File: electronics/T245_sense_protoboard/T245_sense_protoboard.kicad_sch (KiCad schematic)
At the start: 2 parts

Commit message: WIP placement
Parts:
- added C1, C2, C3, C4, C5, C6, C7, C8, C9: 1u, SquantorCapacitor:C_0603, symbol Device:C
- added D1, D2: ~, SquantorIC:SOT23-3, symbol SquantorDiodes:shottky_series
- added J1: Conn_01x06, Connector_Molex:Molex_KK-254_AE-6410-06A_1x06_P2.54mm_Vertical, symbol Connector_Generic:Conn_01x06
- added J2: Conn_02x03_Odd_Even, Connector_Molex:Molex_Micro-Fit_3.0_43045-0612_2x03_P3.00mm_Vertical, symbol Connector_Generic:Conn_02x03_Odd_Even
- added R1, R10, R2, R3, R4: 22K6, SquantorResistor:R_0603_hand, symbol Device:R
- added R11, R12: 10K, SquantorResistor:R_0603_hand, symbol Device:R
- added R13: 187K, SquantorResistor:R_0603_hand, symbol Device:R
- added R14: 3K3, SquantorResistor:R_0603_hand, symbol Device:R
- added R15: 2K2, SquantorResistor:R_0603_hand, symbol Device:R
- added R16, R17: 200K, SquantorResistor:R_0603_hand, symbol Device:R
- added R18, R19: 4k75, SquantorResistor:R_0603_hand, symbol Device:R
- added R20, R21: 0R22, SquantorResistor:R_0805, symbol Device:R
- added R5, R6: 590K, SquantorResistor:R_0603_hand, symbol Device:R
- added R7: 82K, SquantorResistor:R_0603_hand, symbol Device:R
- added R8, R9: 2K7, SquantorResistor:R_0603_hand, symbol Device:R
- added U1: ~, Package_DIP:DIP-16_W7.62mm, symbol SquantorLogic:74XX4053
- added U2, U4: OP07C, Package_DIP:DIP-8_W7.62mm, symbol SquantorGenericAnalog:opamp_single_8pin
- added U3: LM358, Package_DIP:DIP-8_W7.62mm, symbol SquantorGenericAnalog:opamp_dual_8pin
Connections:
- new net: R6.2, R8.1, U2.6 (OUT)
- new net: R7.2, U2.8 (OFS3)
- new net: R1.2, U1.5 (C0)
- new net: R10.1, R9.2, U3.2 (-IN1)
- new net: C8.1, R16.2, R19.1, U4.3 (+IN)
- new net: R19.2, R21.2
- new net: R3.2, U1.2 (B0)
- new net: R20.1, R21.1
- new net: R10.2, R15.2, U3.1 (OUT1)
- new net: R11.1, R17.2, U4.6 (OUT)
- new net: R11.2, U3.5 (+IN2)
- new net: C8.2, R17.1, R18.1, U4.2 (-IN)
- new net: R13.1, R14.1, U3.7 (OUT2)
- new net: R4.2, U1.1 (B1)
- new net: R12.2, R13.2, U3.6 (-IN2)
- new net: R8.2, U3.3 (+IN1)
- new net: R2.2, U1.3 (C1)
- new net +3.3V: C2.2, D1.3, D2.3, J1.3 (Pin_3), U1.16 (VCC)
- new net +5V: J1.4 (Pin_4)
- new net +8V: C4.1, C5.1, C9.1, J1.5 (Pin_5), U2.7 (V+), U3.8 (V+), U4.7 (V+)
- new net -5V: C1.2, C4.2, C5.2, C9.2, J1.1 (Pin_1), U1.7 (VEE), U2.4 (V-), U3.4 (V-), U4.4 (V-)
- new net COM: J2.2 (Pin_2), R3.1
- new net E_out: C7.1, D2.2, R14.2
- new net GND: C1.1, C2.1, C6.2, C7.2, D1.1, D2.1, J1.2 (Pin_2), R12.1, R16.1, R5.1, R7.1, R9.1, U1.11 (S0), U1.6 (!E), U1.8 (GND)
- new net HDL3: J2.3 (Pin_3)
- new net HDL4: J2.4 (Pin_4)
- new net HDL6: J2.6 (Pin_6)
- new net LOAD: J2.5 (Pin_5), R2.1
- new net SEN+: C3.1, R5.2, U1.15 (Bn), U2.3 (+IN)
- new net SEN-: C3.2, R6.1, U1.4 (Cn), U2.2 (-IN)
- new net SW1: U1.9 (S2)
- new net SW2: U1.10 (S1)
- new net TC: J2.1 (Pin_1), R1.1, R18.2, R20.2, R4.1
- new net TC_out: C6.1, D1.2, R15.1
- no-connect marks 0 -> 9

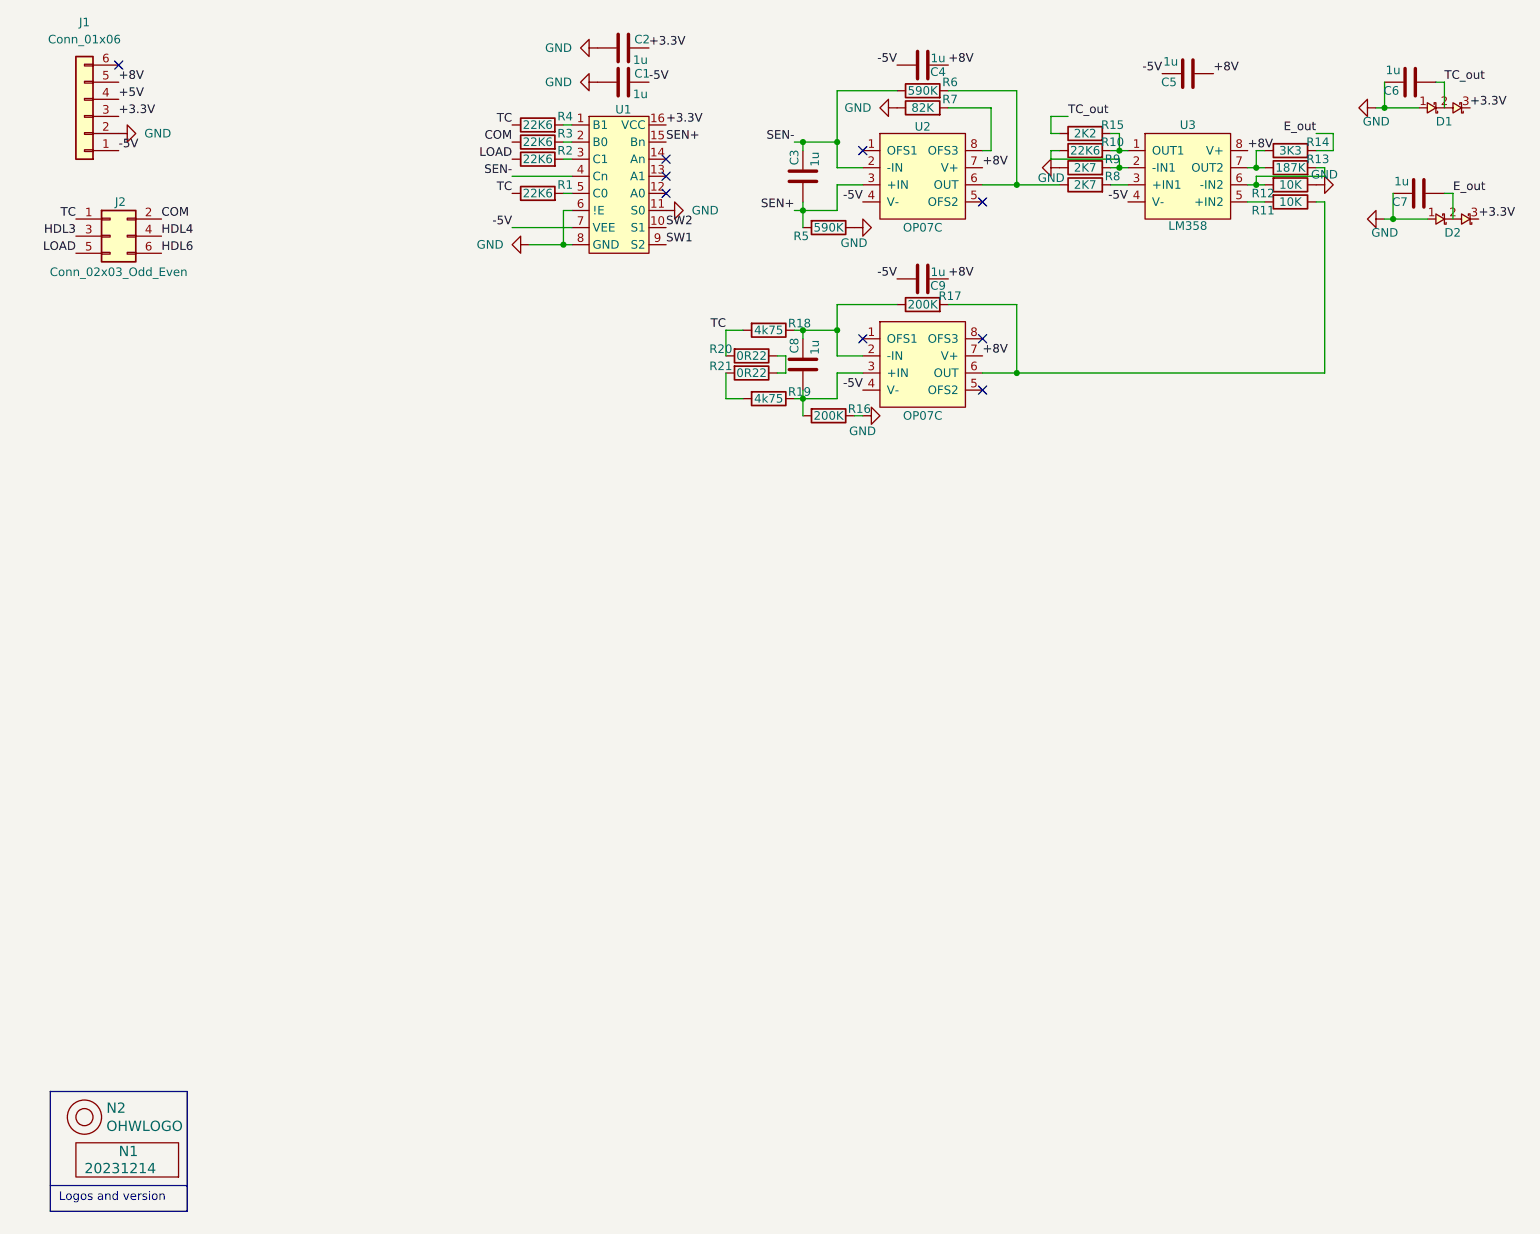
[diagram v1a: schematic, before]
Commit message: switched to dual mux for experiments
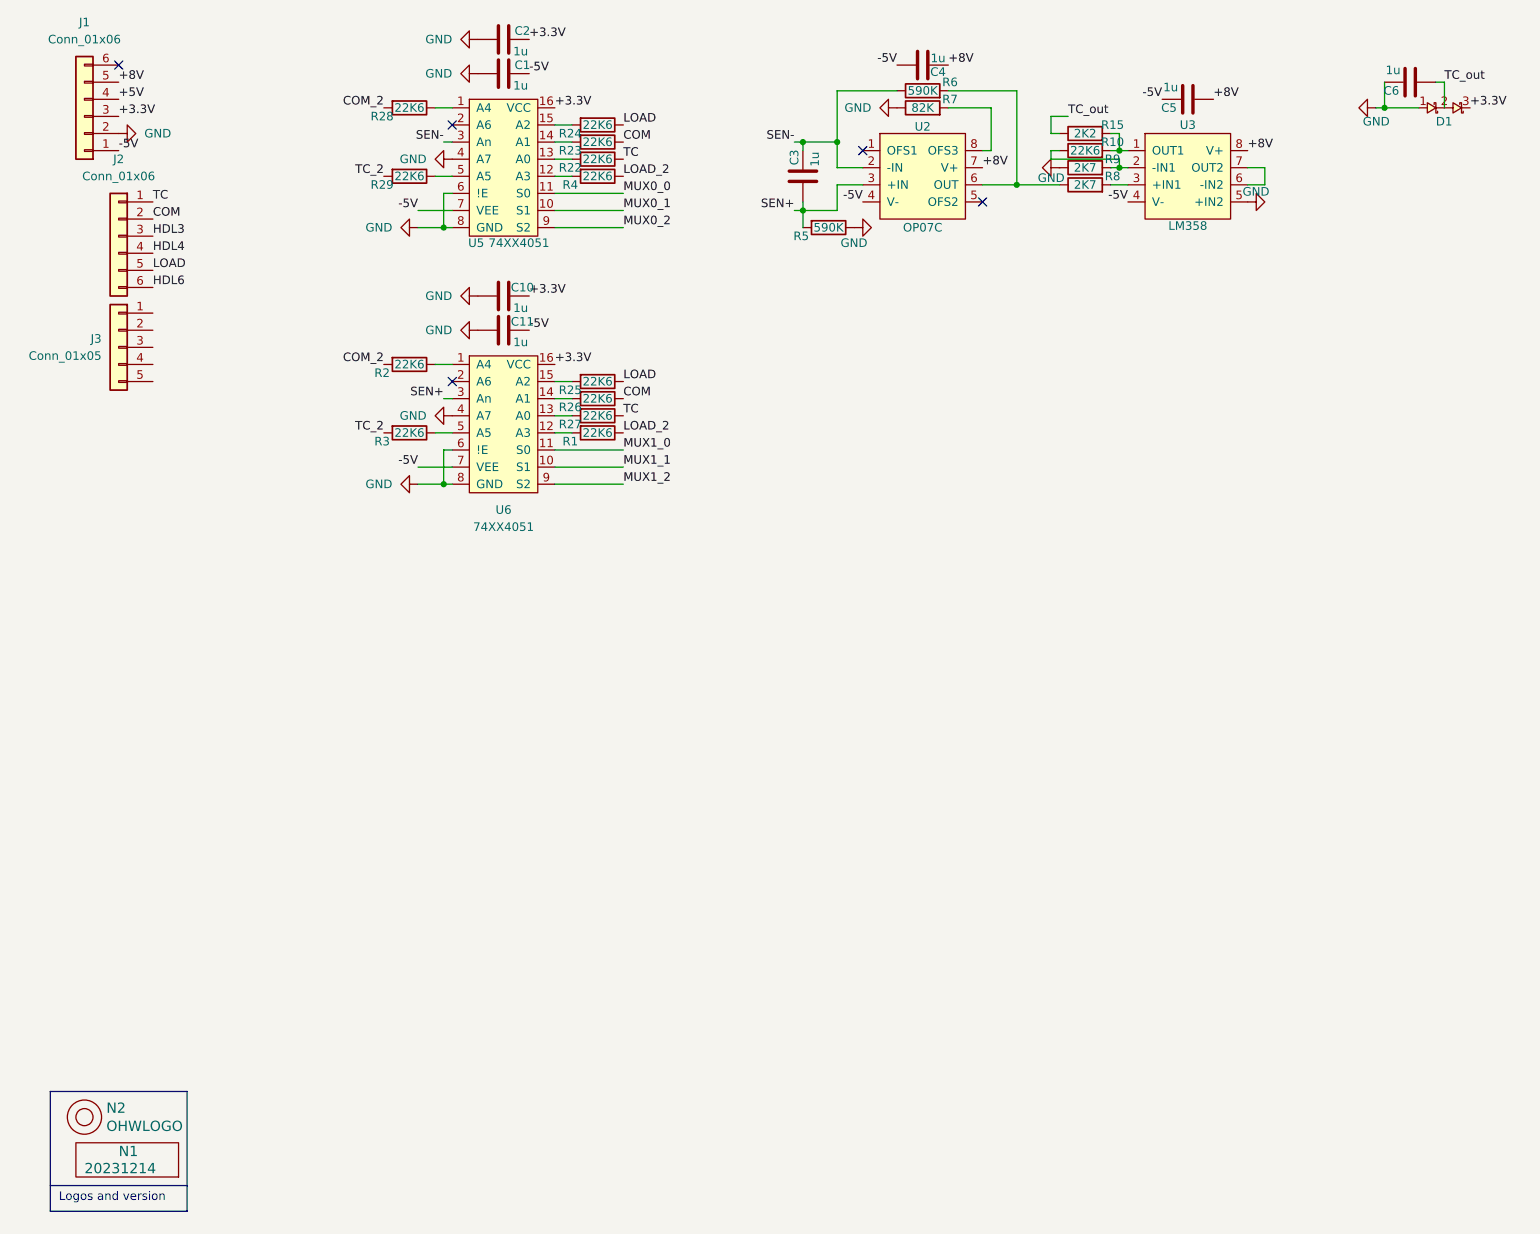
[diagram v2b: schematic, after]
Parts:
- removed C7, C8, C9: 1u, SquantorCapacitor:C_0603, symbol Device:C
- removed D2: ~, SquantorIC:SOT23-3, symbol SquantorDiodes:shottky_series
- removed J2: Conn_02x03_Odd_Even, Connector_Molex:Molex_Micro-Fit_3.0_43045-0612_2x03_P3.00mm_Vertical, symbol Connector_Generic:Conn_02x03_Odd_Even
- removed R11, R12: 10K, SquantorResistor:R_0603_hand, symbol Device:R
- removed R13: 187K, SquantorResistor:R_0603_hand, symbol Device:R
- removed R14: 3K3, SquantorResistor:R_0603_hand, symbol Device:R
- removed R16, R17: 200K, SquantorResistor:R_0603_hand, symbol Device:R
- removed R18, R19: 4k75, SquantorResistor:R_0603_hand, symbol Device:R
- removed R20, R21: 0R22, SquantorResistor:R_0805, symbol Device:R
- removed U1: ~, Package_DIP:DIP-16_W7.62mm, symbol SquantorLogic:74XX4053
- removed U4: OP07C, Package_DIP:DIP-8_W7.62mm, symbol SquantorGenericAnalog:opamp_single_8pin
- added C10, C11: 1u, SquantorCapacitor:C_0603, symbol Device:C
- added J2: Conn_01x06, Connector_JST:JST_XH_B6B-XH-A_1x06_P2.50mm_Vertical, symbol Connector_Generic:Conn_01x06
- added J3: Conn_01x05, Connector_JST:JST_XH_B5B-XH-A_1x05_P2.50mm_Vertical, symbol Connector_Generic:Conn_01x05
- added R22, R23, R24, R25, R26, R27, R28, R29: 22K6, SquantorResistor:R_0603_hand, symbol Device:R
- added U5, U6: 74XX4051, Package_DIP:DIP-16_W7.62mm, symbol SquantorLogic:74XX4051
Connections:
- net +3.3V: now also C10.2, U5.16 (VCC), U6.16 (VCC)
- net -5V: now also C11.2, U5.7 (VEE), U6.7 (VEE)
- net COM: now also J2.2 (Pin_2), R23.1, R26.1; no longer R3.1
- net GND: now also U3.5 (+IN2), C10.1, C11.1, U5.4 (A7), U5.6 (!E), U5.8 (GND), U6.4 (A7), U6.6 (!E), U6.8 (GND)
- net HDL3: now also J2.3 (Pin_3)
- net HDL4: now also J2.4 (Pin_4)
- net HDL6: now also J2.6 (Pin_6)
- net LOAD: now also J2.5 (Pin_5), R24.1, R25.1; no longer R2.1
- net SEN+: now also U6.3 (An)
- net SEN-: now also U5.3 (An)
- net TC: now also J2.1 (Pin_1), R22.1, R27.1; no longer R1.1, R4.1
- net at R1.2: now also U6.12 (A3)
- net TC_2: now reaches R3.2
- net TC_2: now also R29.2
- net at U3.7 (OUT2): now also U3.6 (-IN2)
- net at R4.2: now also U5.12 (A3)
- net COM_2: now reaches R2.2
- net COM_2: now also R28.2
- new net: R29.1, U5.5 (A5)
- new net: R2.1, U6.1 (A4)
- new net: R27.2, U6.13 (A0)
- new net: R26.2, U6.14 (A1)
- new net: R25.2, U6.15 (A2)
- new net: R3.1, U6.5 (A5)
- new net: R22.2, U5.13 (A0)
- new net: R24.2, U5.15 (A2)
- new net: R28.1, U5.1 (A4)
- new net: R23.2, U5.14 (A1)
- new net LOAD_2: R1.1, R4.1
- new net MUX0_0: U5.11 (S0)
- new net MUX0_1: U5.10 (S1)
- new net MUX0_2: U5.9 (S2)
- new net MUX1_0: U6.11 (S0)
- new net MUX1_1: U6.10 (S1)
- new net MUX1_2: U6.9 (S2)
- no-connect marks 9 -> 5
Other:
- moved on the sheet: C1, C2, C5

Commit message: switched mux pinning and additional placing
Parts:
- removed C10, C11: 1u, SquantorCapacitor:C_0603, symbol Device:C
- removed U6: 74XX4051, Package_DIP:DIP-16_W7.62mm, symbol SquantorLogic:74XX4051
- added C7, C8: 1u, SquantorCapacitor:C_0603, symbol Device:C
- added R11, R12, R13, R14, R16, R17, R18: 22K6, SquantorResistor:R_0603_hand, symbol Device:R
- added R19, R20, R21: 47K, SquantorResistor:R_0603_hand, symbol Device:R
- added U1: 74XX4051, Package_DIP:DIP-16_W7.62mm, symbol SquantorLogic:74XX4051
- R25, R26, R27: value 22K6 -> 47K
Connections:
- net +3.3V: now also C7.2, U1.16 (VCC)
- net -5V: now also C8.2, U1.7 (VEE)
- net GND: now also R25.2, R26.2, R27.2, U3.3 (+IN1), C7.1, C8.1, R19.2, R20.2, R21.2, U1.6 (!E), U1.8 (GND); no longer U3.5 (+IN2), U5.4 (A7)
- net MUX0_0: now also R19.1
- net MUX0_1: now also R20.1
- net MUX0_2: now also R21.1
- net MUX1_0: now also R25.1, U1.11 (S0)
- net MUX1_1: now also R26.1, U1.10 (S1)
- net MUX1_2: now also R27.1, U1.9 (S2)
- net SEN+: now also U1.3 (An)
- net at R2.1: now also U1.2 (A6)
- net 2_C2: now reaches R1.2
- net 2_C2: now also J3.3 (Pin_3), R28.2
- net at R3.1: now also U1.4 (A7)
- net at R10.1, R9.2: now also U3.6 (-IN2); no longer U3.2 (-IN1)
- net at R10.2, R15.2: now also U3.7 (OUT2); no longer U3.1 (OUT1)
- net 2_C1: now reaches J3.1 (Pin_1)
- net 2_C1: now also R24.1, R14.1
- net 2_C3B: now reaches J3.2 (Pin_2)
- net 2_C3B: now also R4.1, R18.1
- net 2_C3A: now reaches J3.4 (Pin_4)
- net 2_C3A: now also R29.2, R13.2
- net 2_Sense: now reaches J3.5 (Pin_5)
- net at R8.2: now also U3.5 (+IN2); no longer U3.3 (+IN1)
- net at U5.2 (A6): now also R11.1
- removed net COM: J2.2 (Pin_2), R23.1, R26.1
- net COM_2: no longer names the net of R2.2
- net COM_2: no longer R28.2
- net HDL3 renamed 1_HDL3
- net HDL4 renamed 1_HDL4
- net HDL6 renamed 1_HDL6
- removed net LOAD: J2.5 (Pin_5), R24.1, R25.1
- net LOAD_2: no longer names the net of R1.1
- net LOAD_2: now also U1.1 (A4); no longer R4.1
- net TC renamed 1_TC
- net 1_TC: now also R16.1; no longer R27.1
- net TC_2: no longer names the net of R3.2
- net TC_2: no longer R29.2
- new net: R13.1, U1.5 (A5)
- new net: R12.1, U5.4 (A7)
- new net: R17.2, U1.13 (A0)
- new net: R14.2, U1.15 (A2)
- new net: R16.2, U1.14 (A1)
- new net: R18.2, U1.12 (A3)
- new net: U3.1 (OUT1), U3.2 (-IN1)
- new net 1_COM: J2.2 (Pin_2), R17.1
- new net 1_LOAD: J2.5 (Pin_5), R23.1
- no-connect marks 5 -> 7
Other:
- moved on the sheet: C3, C4, C5, J2, J3, R10, R15, R5, R6, R7, R8, R9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

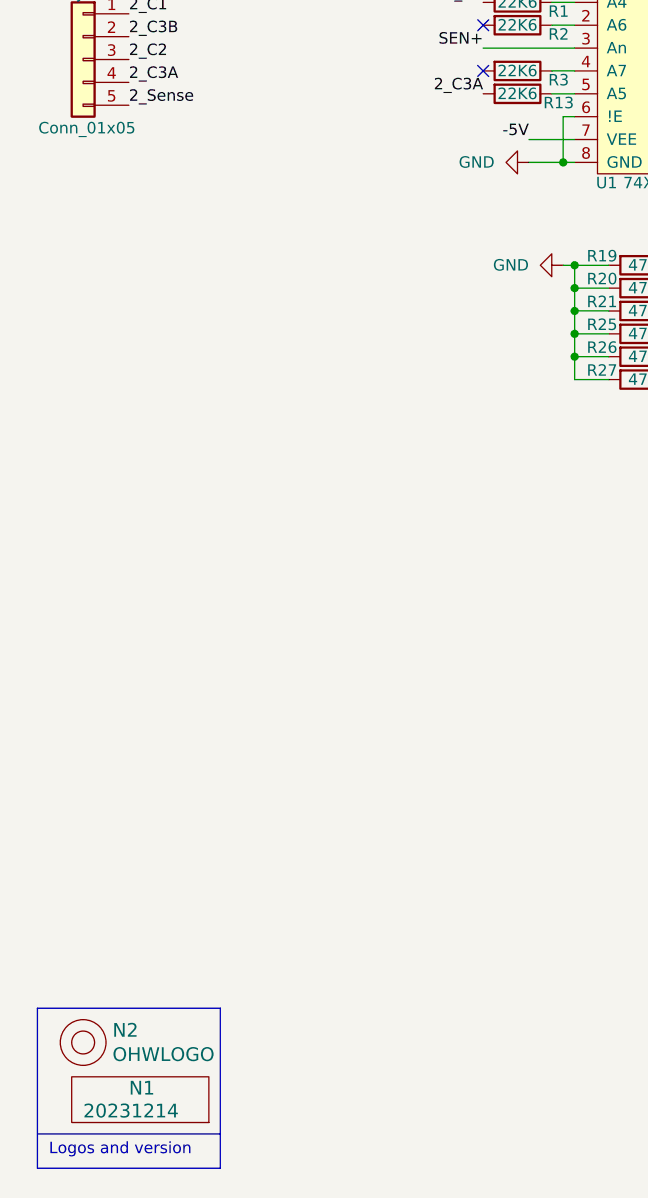
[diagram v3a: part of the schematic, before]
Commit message: protoboard is now 1 on 1 copy of real protoboard
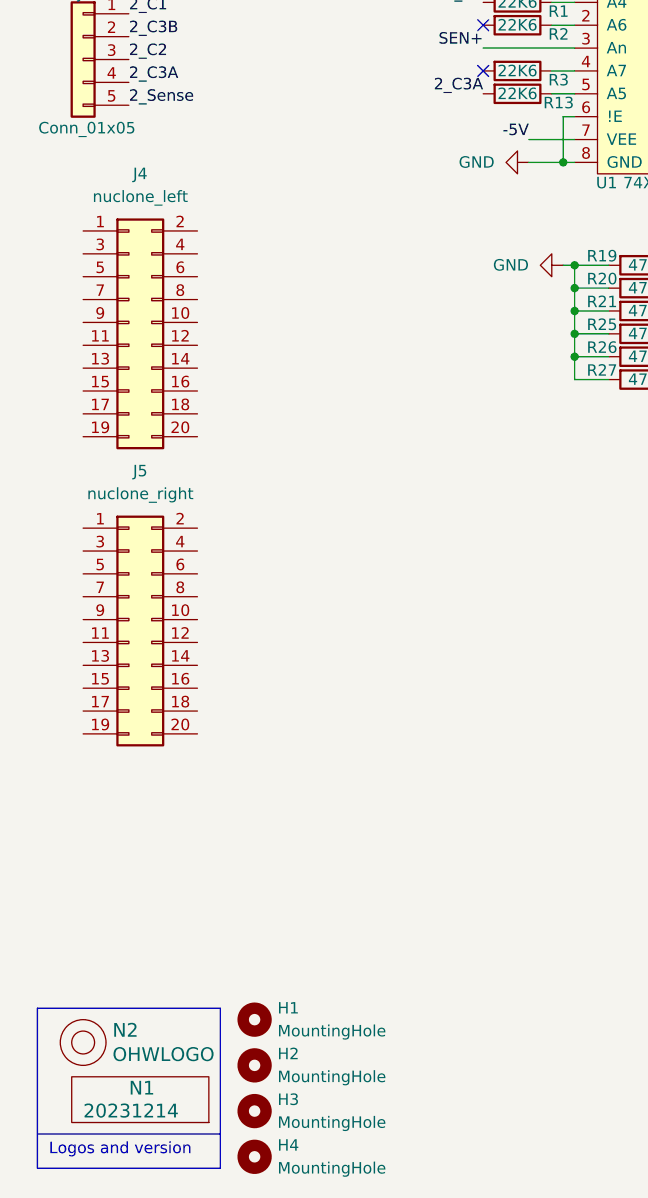
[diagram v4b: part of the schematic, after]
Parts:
- added H1, H2, H3, H4: MountingHole, SquantorPcbOutline:MountingHole_3.2mm_M3_Pad_Via, symbol Mechanical:MountingHole
- added J4: nuclone_left, SquantorConnectors:Header-0254-2X10-H010, symbol Connector_Generic:Conn_02x10_Odd_Even
- added J5: nuclone_right, SquantorConnectors:Header-0254-2X10-H010, symbol Connector_Generic:Conn_02x10_Odd_Even
